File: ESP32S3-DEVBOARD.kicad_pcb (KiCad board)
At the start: 4 copper layers, 33 x 58.4 mm, 61 parts, among them J1 PinHeader_1x22_P2.54mm_Vertic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, J2 PinHeader_1x22_P2.54mm_Vertic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, J3 G-Switch_GT-USB-7010ASV, J4 G-Switch_GT-USB-7010ASV, Q1 BC817-40,215, Q2 BC817-40,215, SW1 TS-1088-AR02016, SW2 TS-1088-AR02016, SW3 TS-1088-AR02016, SW4 TS-1088-AR02016, U1 AMS1117-3.3, U2 ESP32-S3-WROOM-1, U3 USBLC6-2P6, U4 CP2102N-A02-GQFN28R, U5 BMI270, U6 USBLC6-2P6

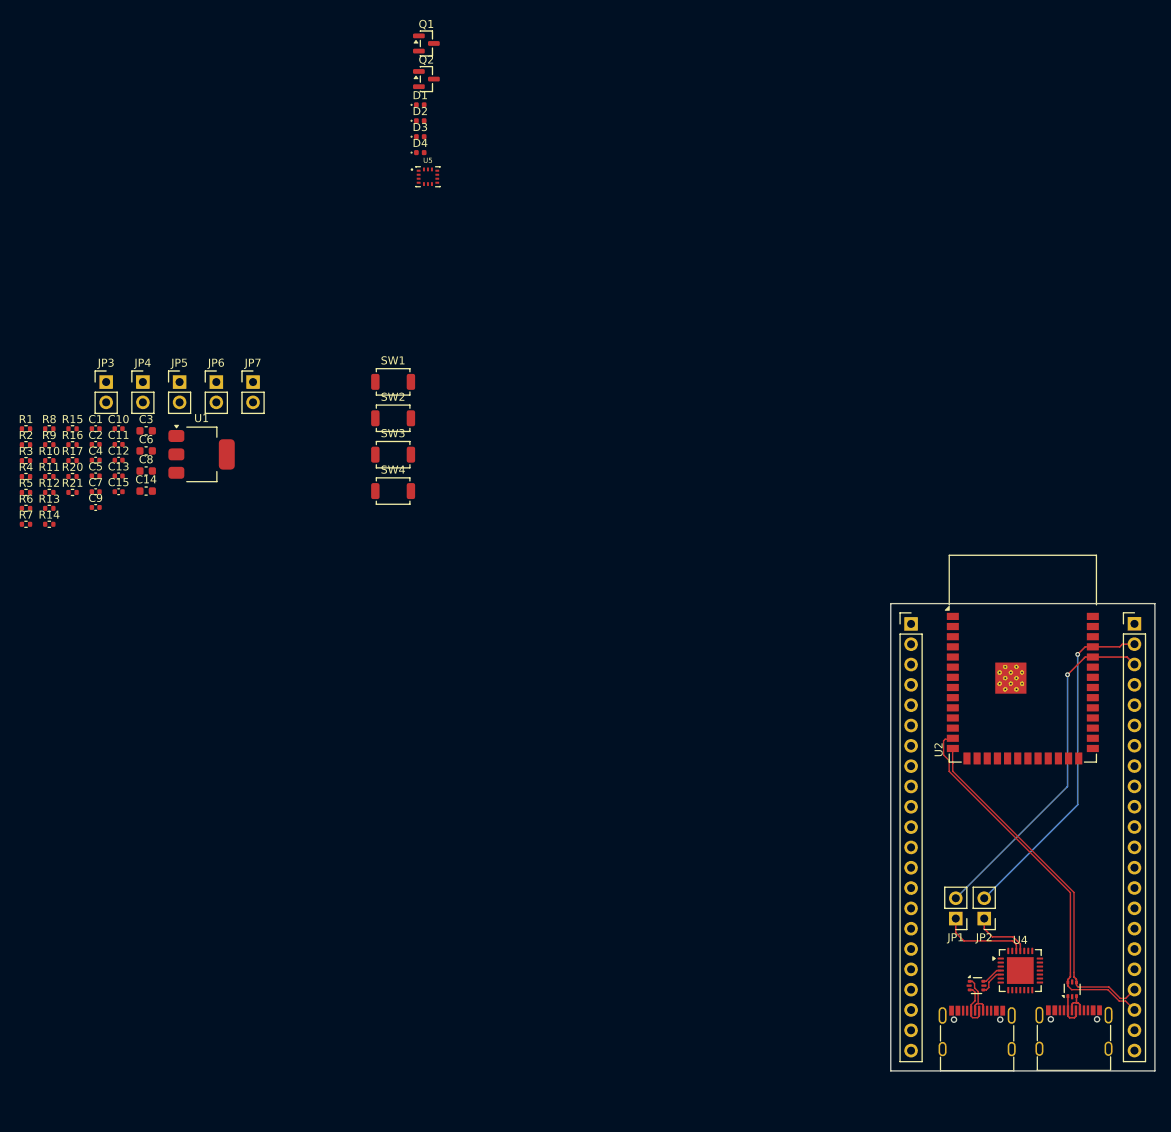
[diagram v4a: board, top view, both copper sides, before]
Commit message: Removed jumpers, and added dipswitch to schematics
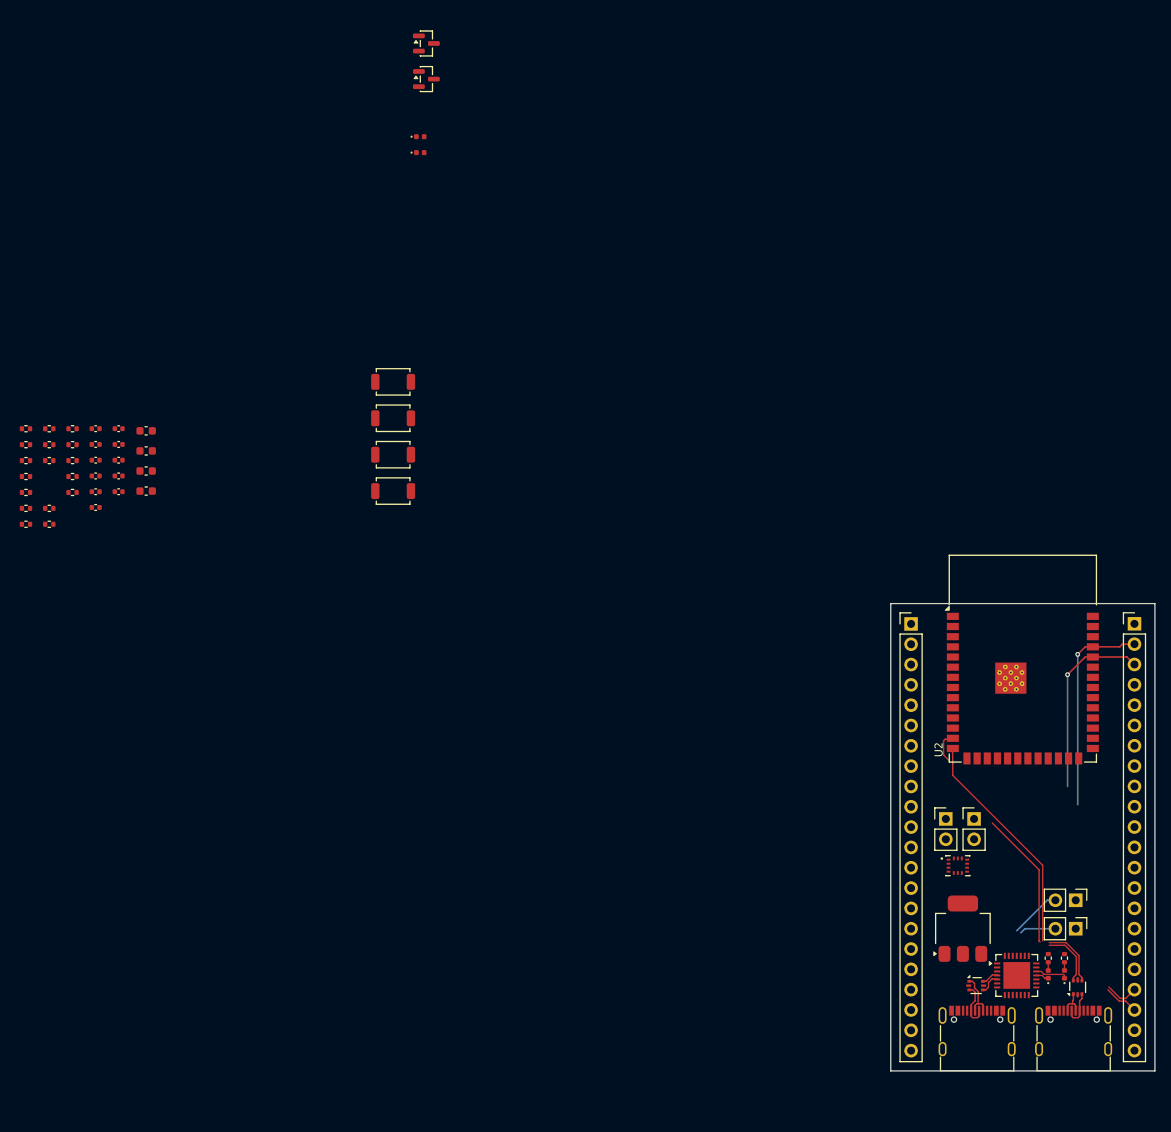
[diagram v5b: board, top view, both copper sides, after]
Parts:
- removed JP5, JP6, JP7: Jumper_1x2_P2.54_Bridged, ESP32S3-DEVBOARD:Jumper_1x02_P2.54mm_Bridged
- moved R11 140.5 mm to (161.4, 143.4), turned to -90 degrees
- moved R12 137.8 mm to (159.4, 143.4), turned to -90 degrees
- moved D1 135.3 mm to (161.4, 145.4), turned to 90 degrees
- moved D2 132.5 mm to (159.4, 145.4), turned to 90 degrees
- moved JP3 121.5 mm to (150.1, 126.0)
- moved JP4 114.3 mm to (146.6, 126.0)
- moved U1 112.1 mm to (148.7, 139.7), turned to 90 degrees
- moved U5 108.6 mm to (148.1, 131.8)
- moved JP1 15.2 mm to (162.8, 136.2), turned to -90 degrees
- moved JP2 11.5 mm to (162.8, 139.7), turned to -90 degrees
- moved U4 0.76 mm to (155.5, 145.6)
- moved U6 0.73 mm to (163.1, 147.0)
- moved J4 0.06 mm to (162.6, 153.7)
- moved U3 0.05 mm to (150.4, 146.8)
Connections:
- net Net-(D1-K) renamed /LED_1
- net Net-(D2-K) renamed /LED_2
- JP1 pad 1: /U2_TX -> /GPIO44
- JP1 pad 2: /GPIO44 -> /U2_TX
- JP2 pad 1: /U2_RX -> /GPIO43
- JP2 pad 2: /GPIO43 -> /U2_RX
- U3 pad 2: GND -> unconnected-(U3-GND-Pad2)
- U3 pad 5: +5V -> unconnected-(U3-VBUS-Pad5)
- U5 pad 12: +3.3V -> Net-(JP5-B)
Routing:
- net /GPIO44: track 43.4 -> 23.6 mm
- net /GPIO43: track 42.9 -> 26.4 mm
- net /USB1_D-: track 48.1 -> 32.8 mm
- net /U2_TX: track 10.8 -> 6.41 mm
- net /LED_1: track 0.00 -> 4.07 mm
- net /USB1_D+: track 44.3 -> 40.5 mm
- net /U2_RX: track 7.44 -> 4.53 mm
- net /LED_2: track 0.00 -> 1.63 mm
- net /USB1_T_D+: track 3.47 -> 4.72 mm
- net Net-(D2-A): track 0.00 -> 1.03 mm
- net Net-(D1-A): track 0.00 -> 1.03 mm
- net /USB1_T_D-: track 4.39 -> 3.75 mm
- net /USB0_D+: track 2.73 -> 2.11 mm
- net /USB0_D-: track 3.35 -> 2.74 mm

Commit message: Changet position of ttl
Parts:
- removed JP1, JP2, JP3, JP4: Jumper_1x2_P2.54_Bridged, ESP32S3-DEVBOARD:Jumper_1x02_P2.54mm_Bridged
- added SW5: SHOU_HAN_1.27-8P_TPPT, ESP32S3-DEVBOARD:SHOU_HAN_1.27-8P_TTPT, F.Cu at (163.3, 132.1)
- moved R9 146.5 mm to (155.8, 161.3)
- moved R17 143.6 mm to (164.7, 147.6), turned to 90 degrees
- moved R16 141.5 mm to (161.3, 147.7), turned to 90 degrees
- moved R20 134.9 mm to (165.8, 125.0), turned to 180 degrees
- moved R21 133.8 mm to (165.8, 122.9), turned to 180 degrees
- moved R10 133.3 mm to (140.0, 162.7)
- moved D4 116.7 mm to (163.6, 125.0)
- moved D3 116.6 mm to (163.6, 122.9)
- moved R3 116.0 mm to (145.4, 103.8)
- moved C2 107.5 mm to (145.4, 101.7)
- moved C7 106.6 mm to (145.4, 102.8)
- moved SW1 95.7 mm to (156.5, 125.4), turned to -90 degrees
- moved SW2 90.2 mm to (152.9, 125.3), turned to -90 degrees
- moved SW3 84.7 mm to (149.4, 125.4), turned to -90 degrees
- moved SW4 79.3 mm to (145.8, 125.4), turned to -90 degrees
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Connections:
- net Net-(JP5-B) renamed /CSB_U5
- J3 pad A5: /CC1 -> /USB_0_CC1
- J3 pad B5: /CC2 -> /USB_0_CC2
- J4 pad A5: /CC1 -> /USB_1_CC1
- J4 pad B5: /CC2 -> /USB_1_CC2
- R16 pad 1: /CC1 -> /USB_1_CC1
- R17 pad 1: /CC2 -> /USB_1_CC2
- R6 pad 1: /CC1 -> /USB_0_CC1
- R7 pad 1: /CC2 -> /USB_0_CC2
- U3 pad 2: unconnected-(U3-GND-Pad2) -> GND
- U3 pad 5: unconnected-(U3-VBUS-Pad5) -> +5V
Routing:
- net /GPIO12: track 0.00 -> 33.8 mm, vias 0 -> 2
- net /GPIO10: track 0.00 -> 26.4 mm, vias 0 -> 2
- net /GPIO11: track 0.00 -> 26.2 mm, vias 0 -> 2
- net /GPIO9: track 0.00 -> 23.4 mm, vias 0 -> 2
- net /GPIO15: track 0.00 -> 21.6 mm, vias 0 -> 1
- net /GPIO46: track 0.00 -> 21.4 mm, vias 0 -> 2
- net /USB1_D+: track 40.5 -> 20.2 mm
- net /GPIO16: track 0.00 -> 18.7 mm, vias 0 -> 1
- net /GPIO44: track 23.6 -> 5.60 mm, vias 1 -> 0
- net /GPIO8: track 0.00 -> 17.8 mm
- net /GPIO3: track 0.00 -> 17.1 mm, vias 0 -> 2
- net /GPIO18: track 0.00 -> 16.7 mm
- net /GPIO17: track 0.00 -> 15.4 mm
- net /GPIO7: track 0.00 -> 12.0 mm
- net /GPIO2: track 0.00 -> 11.8 mm, vias 0 -> 1
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
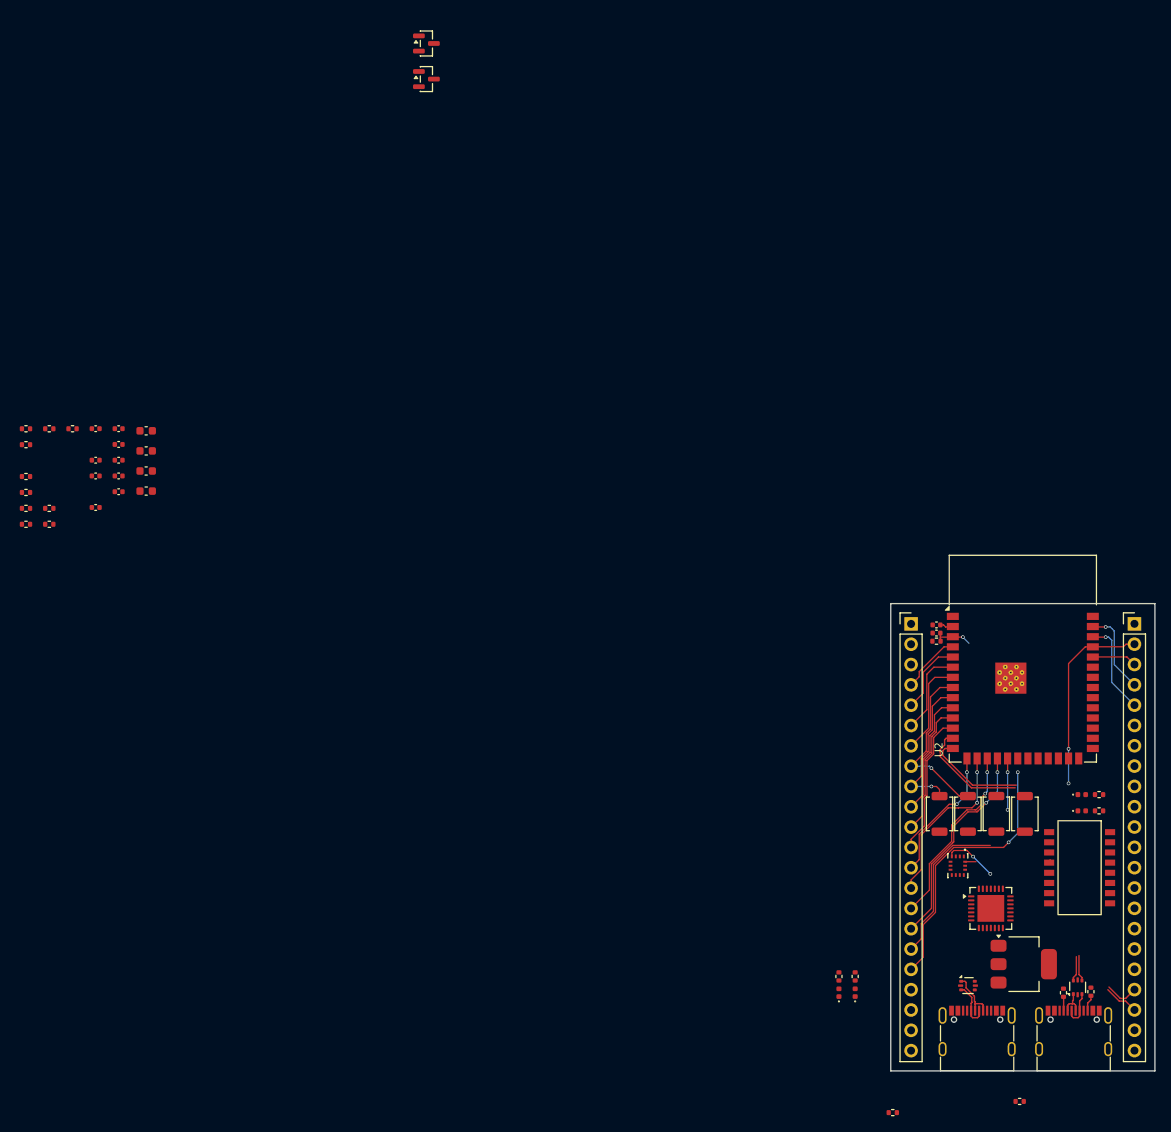
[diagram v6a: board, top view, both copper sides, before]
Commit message: Routing usb for ttl
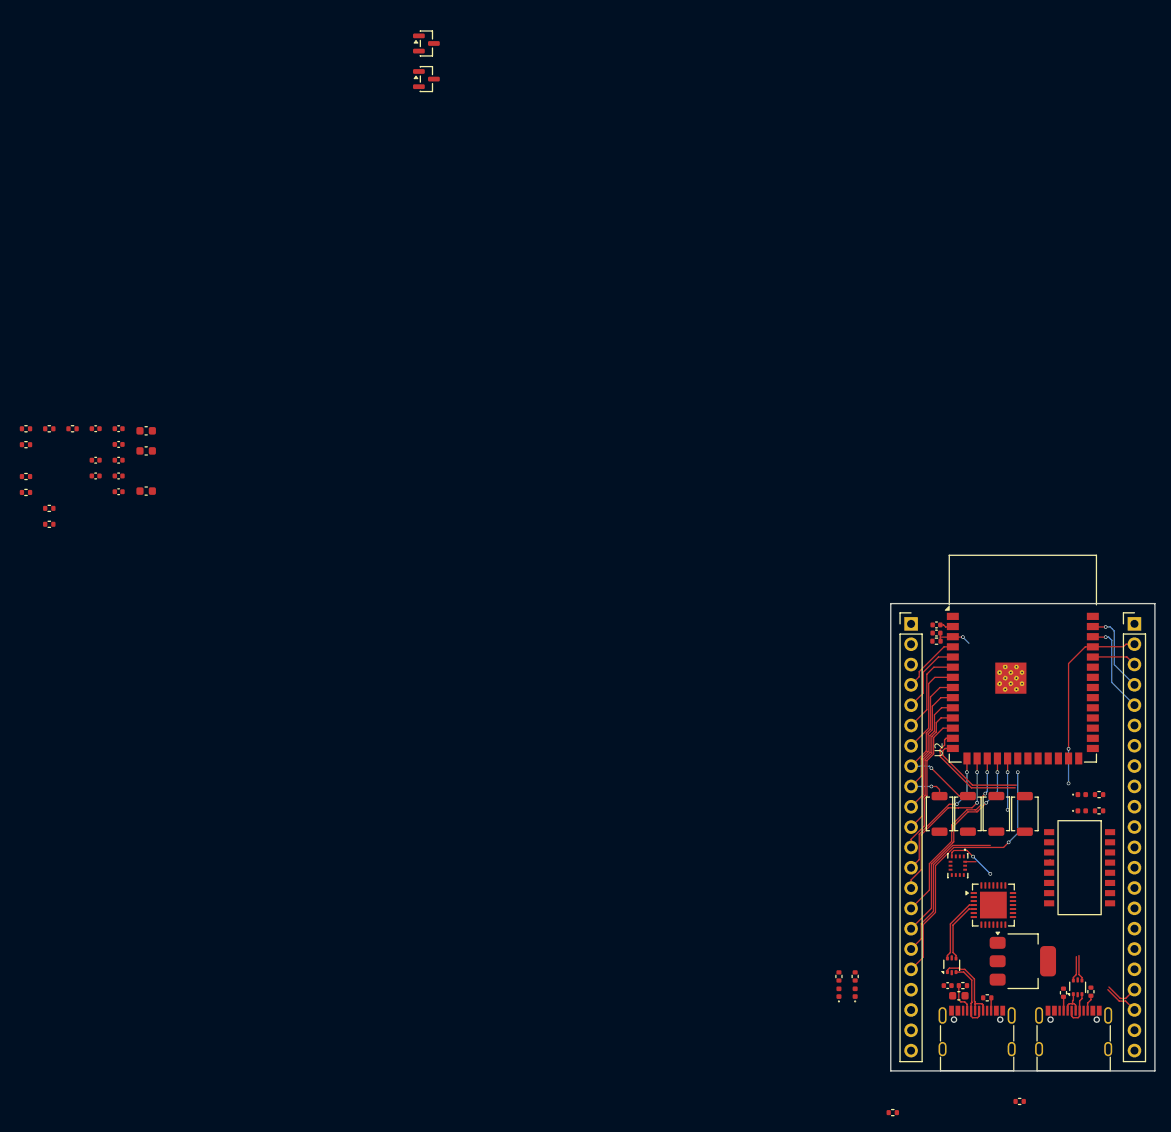
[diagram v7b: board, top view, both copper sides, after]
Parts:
- moved R7 133.9 mm to (151.8, 148.3), turned to 180 degrees
- moved R6 131.4 mm to (148.7, 146.8)
- moved C9 122.1 mm to (146.8, 146.8), turned to 180 degrees
- moved C8 120.9 mm to (148.2, 148.1)
- moved U3 3.25 mm to (147.3, 144.3), turned to 90 degrees
- moved U4 0.53 mm to (152.5, 136.8)
- moved U1 0.38 mm to (156.2, 143.8)
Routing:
- net /USB0_D+: track 0.00 -> 8.37 mm
- net /USB0_D-: track 0.00 -> 7.76 mm
- net /USB_0_CC1: track 0.00 -> 3.84 mm
- net /USB0_T_D+: track 6.46 -> 10.1 mm
- net /USB0_T_D-: track 6.02 -> 8.85 mm
- net /USB_0_CC2: track 0.00 -> 1.62 mm

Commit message: started to wotk on another laptop
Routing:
- net +5V: track 0.00 -> 2.09 mm, vias 0 -> 2
- net GND: track 0.00 -> 1.98 mm, vias 0 -> 2
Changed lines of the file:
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@@
+	)
+	(segment
+		(start 147.335382 145.205374)
+		(end 147.335382 145.549008)
+		(width 0.254)
+		(layer "F.Cu")
+		(net 2)
+	)
+	(segment
+		(start 149.243748 146.441374)
+		(end 148.860748 146.058374)
+		(width 0.254)
+		(layer "F.Cu")
+		(net 2)
+	)
+	(segment
+		(start 149.243748 146.820374)
+		(end 149.243748 146.441374)
+		(width 0.254)
+		(layer "F.Cu")
+		(net 2)
+	)
+	(segment
+		(start 147.335382 145.549008)
+		(end 147.844748 146.058374)
+		(width 0.254)
+		(layer "F.Cu")
+		(net 2)
+	)
+	(via
+		(at 147.844748 146.058374)
+		(size 0.45)
+		(drill 0.3)
+		(layers "F.Cu" "B.Cu")
+		(net 2)
+	)
+	(via
+		(at 148.860748 146.058374)
+		(size 0.45)
+		(drill 0.3)
+		(layers "F.Cu" "B.Cu")
+		(net 2)
+	)
+	(segment
+		(start 147.308748 146.820374)
+		(end 147.308748 146.411374)
+		(width 0.254)
+		(layer "F.Cu")
+		(net 3)
+	)
+	(segment
+		(start 147.450748 148.090374)
+		(end 146.447748 148.090374)
+		(width 0.254)
+		(layer "F.Cu")
+		(net 3)
+	)
+	(segment
+		(start 147.308748 146.411374)
+		(end 146.828748 145.931374)
+		(width 0.254)
+		(layer "F.Cu")
+		(net 3)
+	)
+	(via
+		(at 146.828748 145.931374)
+		(size 0.45)
+		(drill 0.3)
+		(layers "F.Cu" "B.Cu")
+		(net 3)
+	)
+	(via
+		(at 146.447748 148.090374)
+		(size 0.45)
+		(drill 0.3)
+		(layers "F.Cu" "B.Cu")
+		(net 3)
 	)
 	(segment
